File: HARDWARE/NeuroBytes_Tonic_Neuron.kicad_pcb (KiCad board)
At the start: 2 copper layers, 54 x 13.2 mm, 15 parts, among them P1 CONN_01X04, P12 CONN_01X07, U1 STM32L011Gx, U2 LD3985G33R

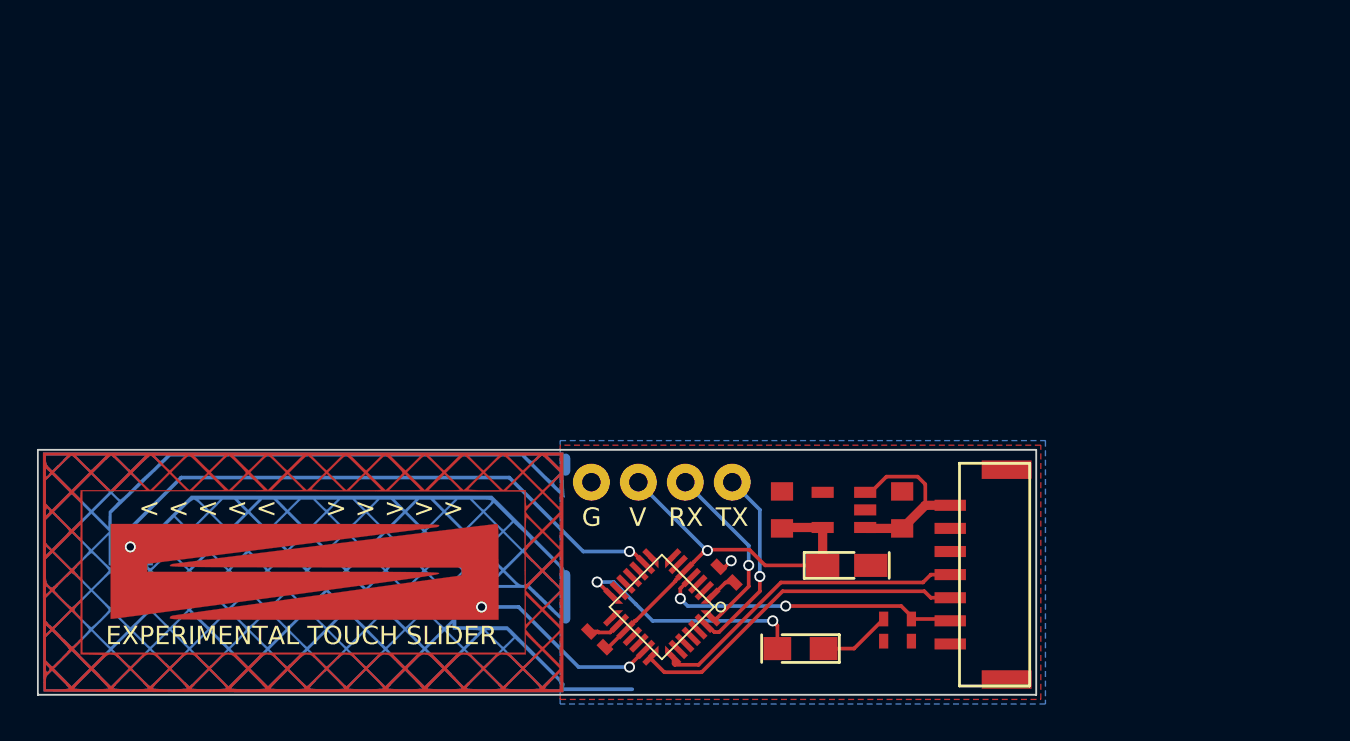
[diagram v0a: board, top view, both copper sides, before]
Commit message: fresh clone with current firmware. added new PCB design -- bipolar neuron graphics, etc.
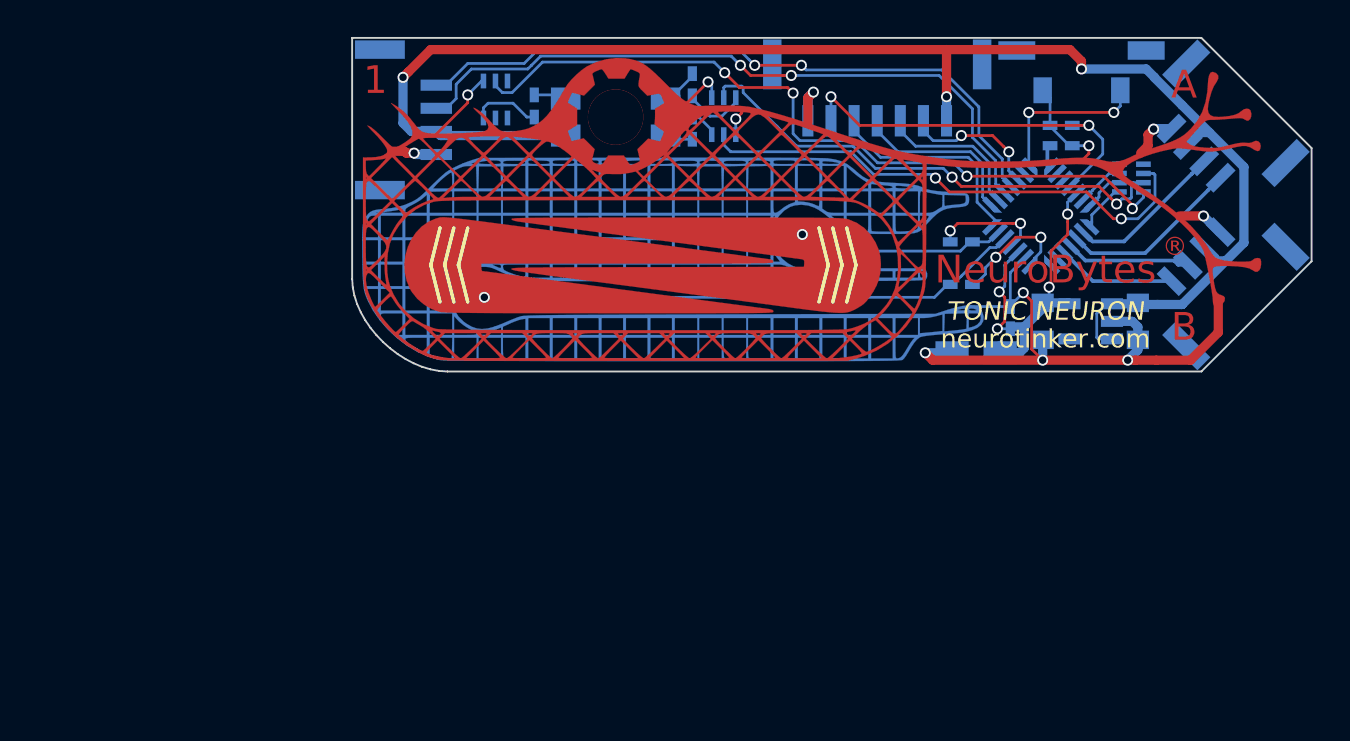
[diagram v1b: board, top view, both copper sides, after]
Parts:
- removed the G*** at (150.7, 89.8)
- added G***: LOGO, KiCad_Footprints:ZF_LOGO_Tonic_Neuron, F.Cu at (167.5, 65.2)
- added P2: CONN_01X04, KiCad_Footprints:ZF_CONN_JST_GH, B.Cu at (200.1, 66.0)
- added P3: CONN_01X04, KiCad_Footprints:ZF_CONN_JST_GH, B.Cu at (200.1, 74.0)
- added Q1: NPN_dual, KiCad_Footprints:ZF_SMD_SOT-363, B.Cu at (173.3, 65.2)
- added Q2: NPN_dual, KiCad_Footprints:ZF_SMD_SOT-363, B.Cu at (161.0, 64.3)
- added R2: 470k, KiCad_Footprints:ZF_SMD_NonPol_0402, B.Cu at (186.2, 74.3)
- added R3: 470k, KiCad_Footprints:ZF_SMD_NonPol_0402, B.Cu at (186.2, 72.0)
- added R5: 100, KiCad_Footprints:ZF_SMD_NonPol_0402, B.Cu at (171.7, 63.5)
- added R6: 100, KiCad_Footprints:ZF_SMD_NonPol_0402, B.Cu at (163.1, 64.7)
- added RN1: R_Pack04, KiCad_Footprints:ZF_RN_4iso_CTS-0804, B.Cu at (195.4, 68.5)
- added SW1: SW_PUSH, KiCad_Footprints:ZF_SW_Momentary_SideMtg, B.Cu at (192.7, 62.9)
- C1, C2, C3, C4, C5, P12, U1, U2: moved to B.Cu
- D1: value LED -> LED_RABG; footprint KiCad_Footprints:ZF_SMD_pol_0805 -> KiCad_Footprints:ZF_LED_RGB_SunLED_XZMDKCBDDG45S-9_cast; moved to B.Cu
- P1: footprint KiCad_Footprints:ZF_CONN_1x4-hdr -> KiCad_Footprints:ZF_CONN_JST_GH; moved to B.Cu
- R1: value R -> 150; moved to B.Cu
- R4: value R -> JMP; moved to B.Cu
- moved D1 30.4 mm to (167.5, 65.2)
- moved U1 29.5 mm to (190.5, 70.6), turned to 315 degrees
- moved R4 29.4 mm to (191.6, 66.8), turned to 180 degrees
- moved R1 29.1 mm to (171.7, 65.8), turned to 90 degrees
- moved C5 28.5 mm to (191.6, 65.7), turned to 180 degrees
- moved C3 28.3 mm to (188.8, 76.1), turned to 90 degrees
- moved P12 26.9 mm to (181.7, 63.9), turned to 90 degrees
- moved TP3 26.6 mm to (177.6, 71.6)
- moved P1 24.0 mm to (156.1, 65.4), turned to 180 degrees
- moved TP4 23.4 mm to (160.4, 75.0)
- moved C4 17.4 mm to (190.6, 76.3), turned to 270 degrees
- moved U2 16.8 mm to (193.2, 76.3), turned to 270 degrees
- moved C1 16.3 mm to (195.8, 76.3), turned to 270 degrees
- moved C2 13.5 mm to (187.0, 78.0), turned to 180 degrees
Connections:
- D1 pad 2: Net-(D1-Pad2) -> +5V
- P1 pad 2: +3V3 -> +5V
- P1 pad 3: USART2_RX -> D1IN
- P1 pad 4: USART2_TX -> D1EX
- P12 pad : GND -> (no net)
- P12 pad 5: Net-(P12-Pad5) -> NSS
- P12 pad 6: Net-(P12-Pad6) -> MOSI
- R1 pad 2: GND -> Net-(Q1-Pad3)
- TP4 pad 1: Net-(TP4-Pad1) -> Net-(R2-Pad1)
- U1 pad 10: Net-(U1-Pad10) -> A1EX
- U1 pad 11: Net-(U1-Pad11) -> A2IN
- U1 pad 12: Net-(U1-Pad12) -> A2EX
- U1 pad 14: Net-(D1-Pad2) -> Net-(U1-Pad14)
- U1 pad 19: Net-(U1-Pad19) -> Net-(R2-Pad1)
- U1 pad 23: Net-(U1-Pad23) -> NSS
- U1 pad 24: Net-(U1-Pad24) -> D1IN
- U1 pad 25: Net-(U1-Pad25) -> D1EX
- U1 pad 26: Net-(U1-Pad26) -> MOSI
- U1 pad 27: USART2_TX -> Net-(U1-Pad27)
- U1 pad 28: USART2_RX -> Net-(SW1-Pad2)
- U1 pad 6: Net-(U1-Pad6) -> LED_R
- U1 pad 7: Net-(U1-Pad7) -> LED_G
- U1 pad 8: Net-(U1-Pad8) -> LED_B
- U1 pad 9: Net-(TP4-Pad1) -> A1IN
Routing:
- net +5V: track 10.1 -> 83.2 mm, vias 0 -> 3
- net GND: track 2.66 -> 61.0 mm, vias 1 -> 12
- net Net-(Q2-Pad5): track 0.00 -> 41.4 mm, vias 0 -> 4
- net D1IN: track 0.00 -> 37.1 mm, vias 0 -> 2
- net D1EX: track 0.00 -> 37.0 mm, vias 0 -> 2
- net Net-(TP4-Pad1): track 32.0 -> 0.00 mm, vias 2 -> 0
- net Net-(R2-Pad1): track 0.00 -> 29.5 mm, vias 0 -> 1
- net Net-(Q1-Pad2): track 0.00 -> 28.0 mm, vias 0 -> 2
- net Net-(Q1-Pad5): track 0.00 -> 27.1 mm, vias 0 -> 2
- net Net-(D1-Pad2): track 13.0 -> 0.00 mm, vias 2 -> 0
- net USART2_TX: track 10.6 -> 0.00 mm, vias 1 -> 0
- net A1EX: track 0.00 -> 9.79 mm
- net USART2_RX: track 9.73 -> 0.00 mm, vias 1 -> 0
- net Net-(SW1-Pad2): track 0.00 -> 9.36 mm, vias 0 -> 2
- net A1IN: track 0.00 -> 8.54 mm
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- removed copper zone on B.Cu, net GND
- removed copper zone on F.Cu, net GND
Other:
- board size 54 x 13.2 mm -> 51.9 x 18 mm
- net class Default: clearance 0.2 -> 0.14; trace_width 0.2 -> 0.15
- rule trace_clearance: 0.2 -> 0.14
- rule trace_min: 0.2 -> 0.15
- board text added: "1"
- board text added: "A"
- board text added: "B"
- board text added: "ID"
- board text added: "NeuroBytes"
- board text added: "TONIC NEURON"
- board text added: "neurotinker.com"
- board text added: "®"
- board text removed: "< < < < < > > > > >"
- board text removed: "EXPERIMENTAL TOUCH SLIDER"
- board text removed: "G"
- board text removed: "RX"
- board text removed: "TX"
- board text removed: "V"

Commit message: removed miniprintf stuff. updated firmware for new board with external resistors for touch slider. currently runs test program that maps finger position to blue LED color.
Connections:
- RN1 pad 2: LED_R -> LED_G
- RN1 pad 3: LED_G -> LED_R
- U1 pad 6: LED_R -> LED_G
- U1 pad 7: LED_G -> LED_R
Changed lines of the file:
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@@
     (links 75)
     (no_connects 8)
-    (area 151.126667 58.385002 208.589752 82.489752)
+    (area 153.199999 60.917456 205.198036 79.062409)
     (thickness 1.6)
     (drawings 44)
@@
       (net 3 +3V3))
     (pad 6 smd rect (at 1 -2.25 135) (size 0.3 1.2) (layers B.Cu B.Paste B.Mask)
+      (net 32 LED_G))
+    (pad 7 smd rect (at 1.5 -2.4 135) (size 0.3 0.9) (layers B.Cu B.Paste B.Mask)
       (net 31 LED_R))
-    (pad 7 smd rect (at 1.5 -2.4 135) (size 0.3 0.9) (layers B.Cu B.Paste B.Mask)
-      (net 32 LED_G))
     (pad 8 smd rect (at 2.4 -1.5 45) (size 0.3 0.9) (layers B.Cu B.Paste B.Mask)
       (net 33 LED_B))
@@
       (net 27 "Net-(R2-Pad2)"))
     (pad 7 smd trapezoid (at 1.5 -2 315) (size 0.3 0.5) (rect_delta 0.3 0 ) (layers B.Cu B.Paste B.Mask)
-      (net 32 LED_G))
+      (net 31 LED_R))
     (pad 8 smd trapezoid (at 2 -1.5 45) (size 0.3 0.5) (rect_delta 0.3 0 ) (layers B.Cu B.Paste B.Mask)
       (net 33 LED_B))
@@
       (net 41 "Net-(RN1-Pad1)"))
     (pad 2 smd rect (at -0.65 -0.25 270) (size 0.3 0.8) (layers B.Cu B.Paste B.Mask)
+      (net 32 LED_G))
+    (pad 3 smd rect (at -0.65 0.25 270) (size 0.3 0.8) (layers B.Cu B.Paste B.Mask)
       (net 31 LED_R))
-    (pad 3 smd rect (at -0.65 0.25 270) (size 0.3 0.8) (layers B.Cu B.Paste B.Mask)
-      (net 32 LED_G))
     (pad 4 smd rect (at -0.65 0.75 270) (size 0.3 0.8) (layers B.Cu B.Paste B.Mask)
       (net 33 LED_B))
@@
   (segment (start 190.853553 66.946447) (end 191 66.8) (width 0.2) (layer B.Cu) (net 30))
   (segment (start 191.2 67.77868) (end 191.136396 67.842284) (width 0.2) (layer B.Cu) (net 30))
-  (segment (start 192.798097 69.716117) (end 193.293071 69.221143) (width 0.15) (layer B.Cu) (net 31))
-  (segment (start 193.293071 69.221143) (end 193.293071 69.206929) (width 0.15) (layer B.Cu) (net 31))
-  (segment (start 193.293071 69.206929) (end 194.2 68.3) (width 0.15) (layer B.Cu) (net 31))
-  (segment (start 194.2 68.3) (end 194.75 68.3) (width 0.15) (layer B.Cu) (net 31))
-  (segment (start 193.257716 69.963604) (end 193.646624 69.574696) (width 0.15) (layer B.Cu) (net 32))
-  (segment (start 193.646624 69.574696) (end 193.646624 69.353376) (width 0.15) (layer B.Cu) (net 32))
-  (segment (start 193.646624 69.353376) (end 194.2 68.8) (width 0.15) (layer B.Cu) (net 32))
-  (segment (start 194.2 68.8) (end 194.75 68.8) (width 0.15) (layer B.Cu) (net 32))
-  (segment (start 193.257716 69.963604) (end 193.257716 69.942284) (width 0.2) (layer B.Cu) (net 32))
+  (segment (start 193.257716 69.963604) (end 193.646624 69.574696) (width 0.15) (layer B.Cu) (net 31))
+  (segment (start 193.646624 69.574696) (end 193.646624 69.353376) (width 0.15) (layer B.Cu) (net 31))
+  (segment (start 193.646624 69.353376) (end 194.2 68.8) (width 0.15) (layer B.Cu) (net 31))
+  (segment (start 194.2 68.8) (end 194.75 68.8) (width 0.15) (layer B.Cu) (net 31))
+  (segment (start 193.257716 69.963604) (end 193.257716 69.942284) (width 0.2) (layer B.Cu) (net 31))
+  (segment (start 192.798097 69.716117) (end 193.293071 69.221143) (width 0.15) (layer B.Cu) (net 32))
+  (segment (start 193.293071 69.221143) (end 193.293071 69.206929) (width 0.15) (layer B.Cu) (net 32))
+  (segment (start 193.293071 69.206929) (end 194.2 68.3) (width 0.15) (layer B.Cu) (net 32))
+  (segment (start 194.2 68.3) (end 194.75 68.3) (width 0.15) (layer B.Cu) (net 32))
   (segment (start 194.75 69.3) (end 194.5 69.3) (width 0.15) (layer B.Cu) (net 33))
   (segment (start 194.5 69.3) (end 193.257716 70.542284) (width 0.15) (layer B.Cu) (net 33))

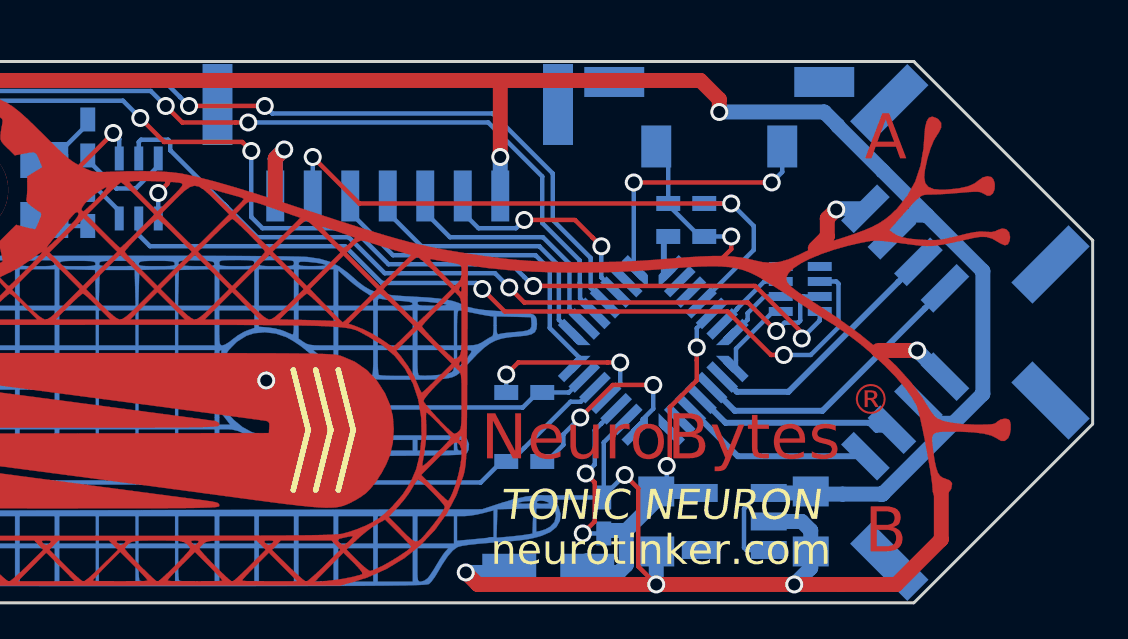
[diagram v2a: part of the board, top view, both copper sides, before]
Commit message: changed to 5-pin JST GH connector for power / prog
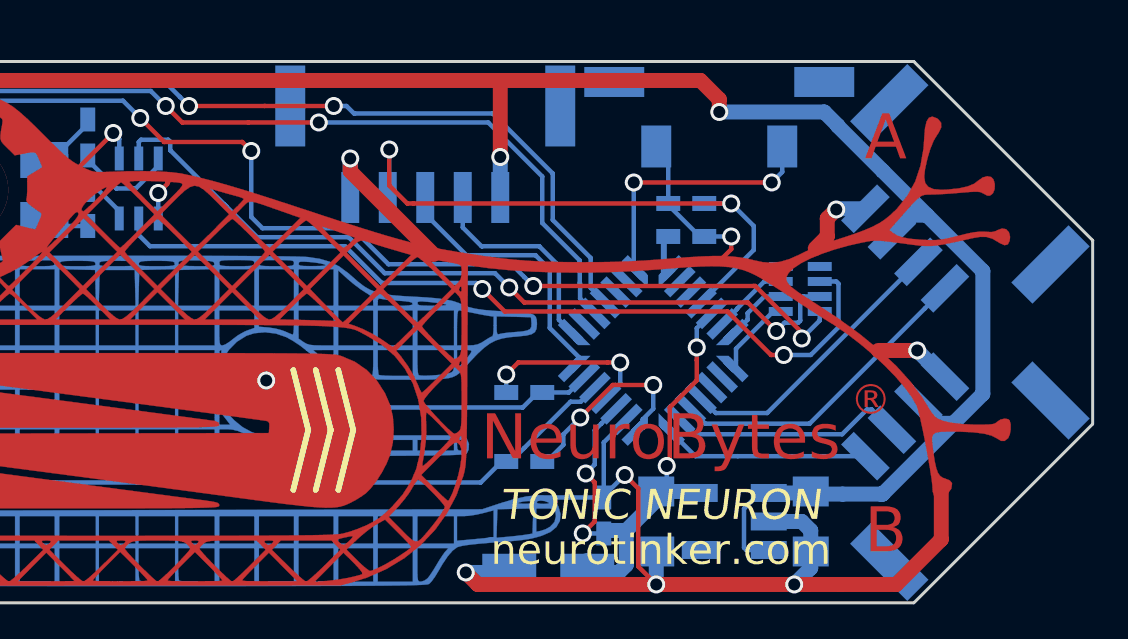
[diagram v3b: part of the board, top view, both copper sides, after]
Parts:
- removed P12: CONN_01X07, KiCad_Footprints:ZF_CONN_JST_GH_7POS
- added P4: JST_GH_5-pos, KiCad_Footprints:ZF_CONN_JST_GH_5POS, B.Cu at (182.9, 63.9)
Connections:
- U1 pad 10: A1EX -> Net-(U1-Pad10)
- U1 pad 11: A2IN -> A1IN
- U1 pad 12: A2EX -> A1EX
- U1 pad 13: Net-(U1-Pad13) -> A2IN
- U1 pad 14: Net-(U1-Pad14) -> A2EX
- U1 pad 21: SWDIO/SCK -> SWDIO
- U1 pad 22: SWCLK/MISO -> SWCLK
- U1 pad 23: NSS -> Net-(U1-Pad23)
- U1 pad 26: MOSI -> Net-(U1-Pad26)
- U1 pad 9: A1IN -> Net-(U1-Pad9)
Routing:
- net SWDIO/SCK: track 11.4 -> 0.00 mm
- net SWCLK/MISO: track 9.34 -> 0.00 mm
- net SWDIO: track 0.00 -> 8.92 mm
- net NSS: track 8.28 -> 0.00 mm
- net MOSI: track 7.67 -> 0.00 mm, vias 2 -> 0
- net SWCLK: track 0.00 -> 7.08 mm
- net GND: track 61.0 -> 63.1 mm
- net RESET: track 21.1 -> 19.7 mm
- net A2IN: track 6.80 -> 7.90 mm
- net A1IN: track 8.54 -> 9.54 mm
- net A1EX: track 9.79 -> 10.6 mm
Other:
- board text added: "POWER"

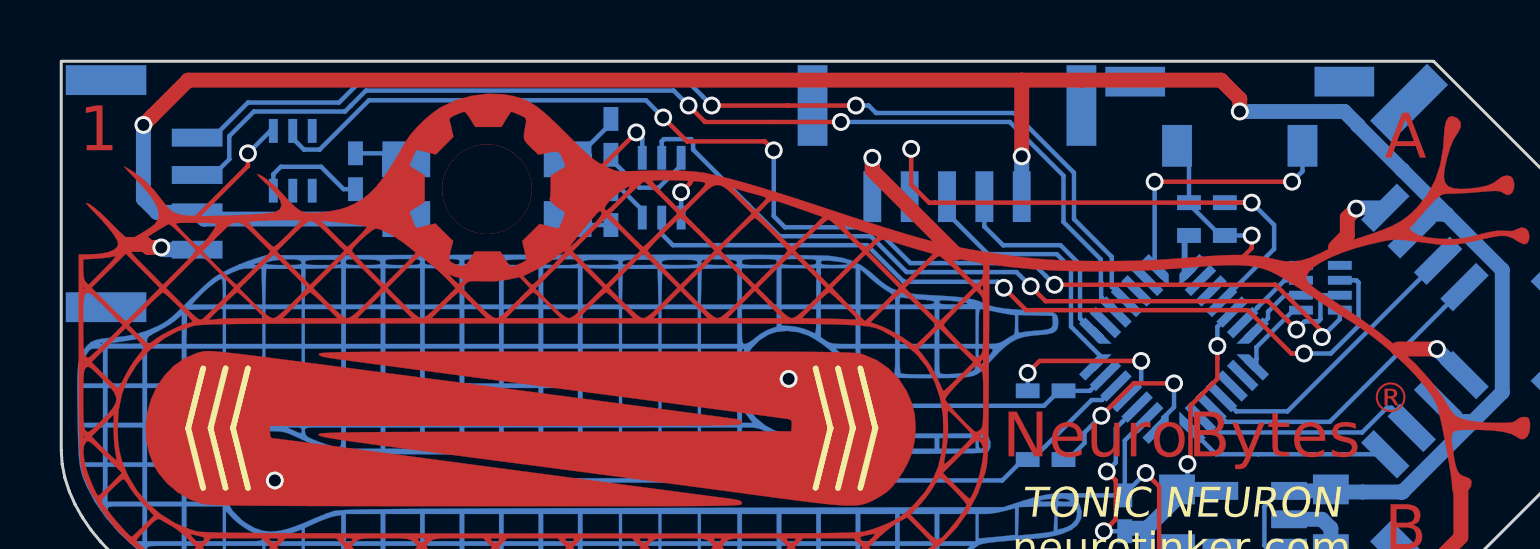
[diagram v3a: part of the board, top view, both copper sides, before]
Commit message: changed to single NPN transitors and non-networked resistors. still need to finish routing.
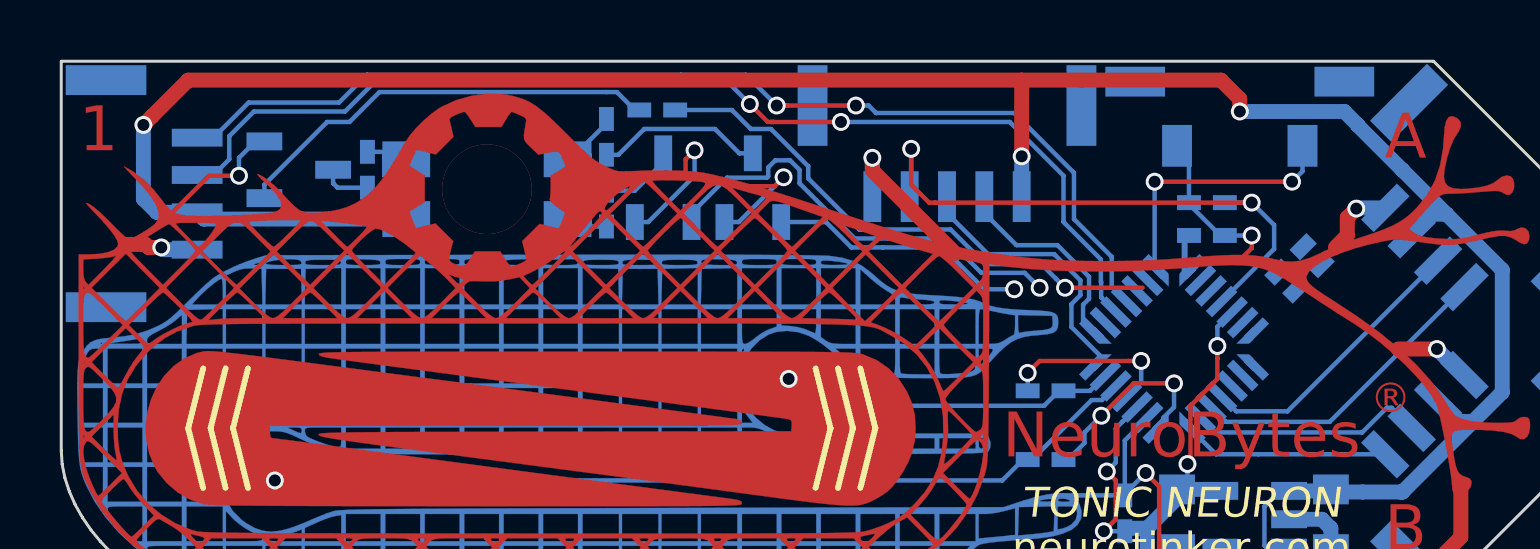
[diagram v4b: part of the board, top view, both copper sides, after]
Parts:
- removed RN1: R_Pack04, KiCad_Footprints:ZF_RN_4iso_CTS-0804
- added Q3: Q_NPN_BEC, KiCad_Footprints:ZF_SOT23-3L, B.Cu at (161.2, 64.6)
- added R7: 1k, KiCad_Footprints:ZF_SMD_NonPol_0402, B.Cu at (195.0, 68.2)
- added R8: 1k, KiCad_Footprints:ZF_SMD_NonPol_0402, B.Cu at (194.4, 67.6)
- added R9: 1k, KiCad_Footprints:ZF_SMD_NonPol_0402, B.Cu at (173.2, 62.6)
- C2: value CP -> 10u; footprint KiCad_Footprints:ZF_SMD_pol_1206 -> KiCad_Footprints:ZF_SMD_nonpol_1206
- Q1, Q2: value NPN_dual -> Q_NPN_BEC; footprint KiCad_Footprints:ZF_SMD_SOT-363 -> KiCad_Footprints:ZF_SOT23-3L
- moved Q2 15.4 mm to (176.4, 65.2), turned to 0 degrees
- moved R6 0.40 mm to (163.5, 64.6)
- moved R1 0.16 mm to (171.5, 65.9)
- moved R5 0.15 mm to (171.5, 63.5)
- moved Q1 0.05 mm to (173.4, 65.2), turned to 0 degrees
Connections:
- Q1 pad 1: GND -> Net-(Q1-Pad1)
- Q1 pad 2: Net-(Q1-Pad2) -> GND
- Q2 pad 2: Net-(Q2-Pad2) -> GND
- R5 pad 2: Net-(Q1-Pad6) -> Net-(Q2-Pad3)
- R6 pad 2: Net-(Q2-Pad3) -> Net-(Q3-Pad3)
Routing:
- net Net-(Q2-Pad5): track 41.4 -> 0.00 mm, vias 4 -> 0
- net Net-(Q1-Pad2): track 28.0 -> 0.00 mm, vias 2 -> 0
- net Net-(Q1-Pad5): track 27.1 -> 0.00 mm, vias 2 -> 0
- net LED_B: track 2.70 -> 18.4 mm, vias 0 -> 1
- net Net-(Q1-Pad1): track 0.00 -> 14.9 mm, vias 0 -> 1
- net Net-(Q3-Pad1): track 0.00 -> 14.5 mm
- net Net-(Q2-Pad1): track 0.00 -> 8.73 mm, vias 0 -> 1
- net GND: track 63.1 -> 67.3 mm
- net Net-(Q1-Pad6): track 3.45 -> 0.00 mm
- net LED_G: track 2.55 -> 0.00 mm
- net LED_R: track 2.13 -> 0.02 mm
- net Net-(Q2-Pad3): track 3.71 -> 5.60 mm
- net Net-(Q3-Pad3): track 0.00 -> 1.66 mm
- net Net-(Q1-Pad3): track 1.59 -> 2.59 mm
- net Net-(D1-Pad1): track 2.08 -> 2.62 mm
